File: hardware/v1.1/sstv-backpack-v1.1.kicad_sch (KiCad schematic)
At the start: 23 parts, among them J1 Conn_01x03_Pin, J2 Conn_01x02_Pin, J4 USB_C_Receptacle_USB2.0_14P, Q2 2N3904, SW1 SW_Push, SW2 SLW-1276864-4A-D, U1 ESP32-CAM, U2 FT231XS

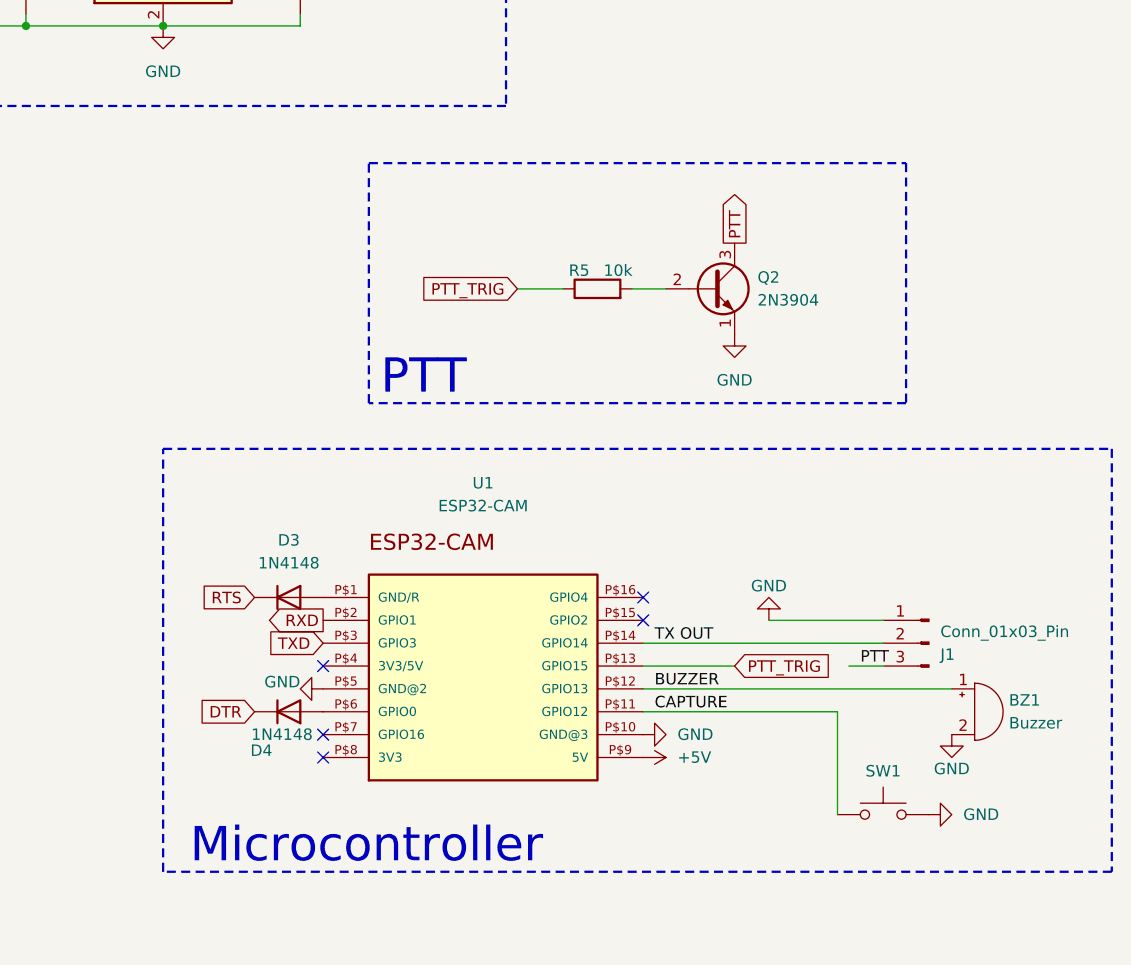
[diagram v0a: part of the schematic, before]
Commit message: Update README and add pull-down resistors for PTT
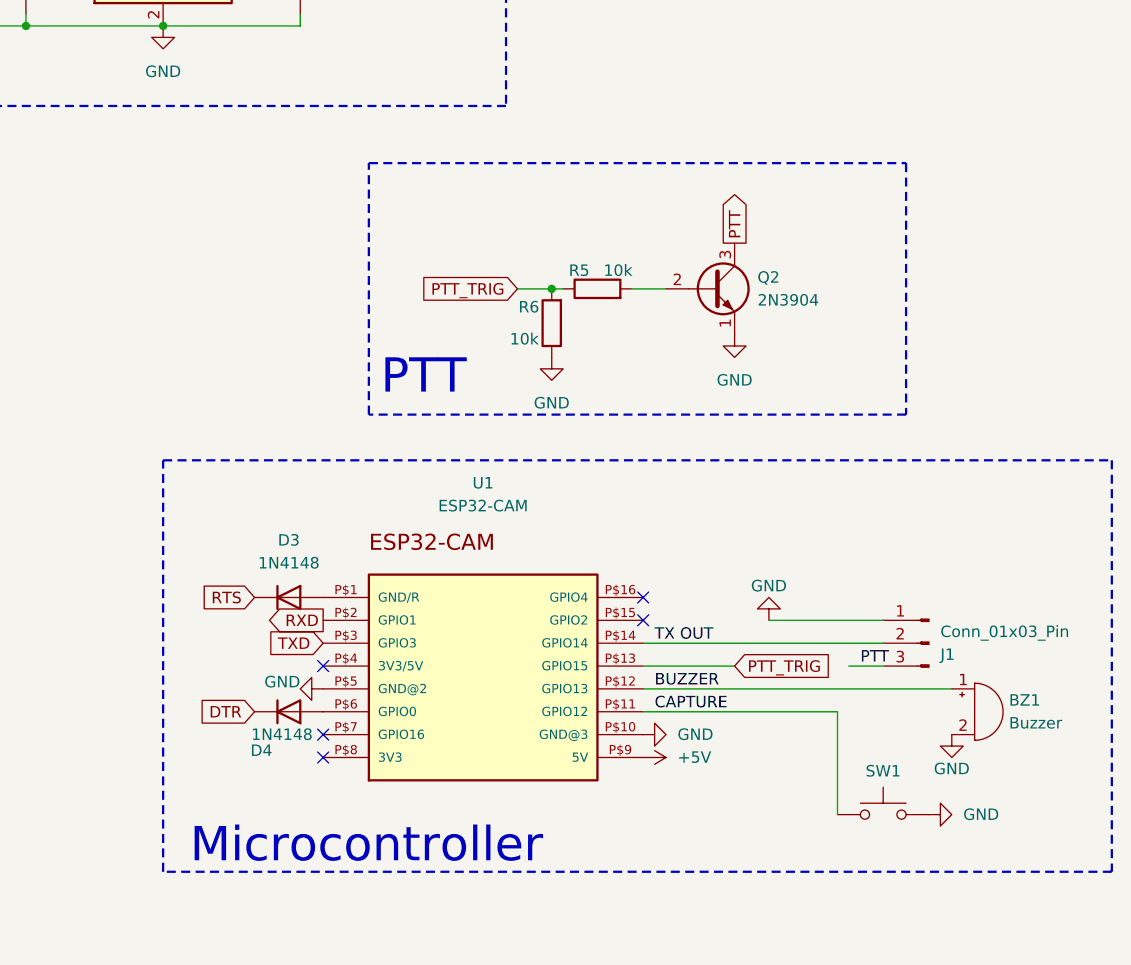
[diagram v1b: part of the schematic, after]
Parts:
- added R6: 10k, Resistor_THT:R_Axial_DIN0207_L6.3mm_D2.5mm_P7.62mm_Horizontal, symbol Device:R
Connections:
- net GND: now also R6.1
- net PTT_TRIG: now also R6.2
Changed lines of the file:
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@@
 	)
 	(rectangle
-		(start 163.83 109.22)
+		(start 163.83 110.49)
 		(end 269.24 156.21)
 		(stroke
@@
 	(rectangle
 		(start 186.69 77.47)
-		(end 246.38 104.14)
+		(end 246.38 105.41)
 		(stroke
 			(width 0.25)
@@
 	)
 	(junction
+		(at 207.01 91.44)
+		(diameter 0)
+		(color 0 0 0 0)
+	)
+	(junction
 		(at 179.07 52.07)
 		(diameter 0)
@@
 	(wire
 		(pts
+			(xy 207.01 91.44) (xy 208.28 91.44)
+		)
+		(stroke
+			(width 0)
+			(type default)
+		)
+	)
+	(wire
+		(pts
 			(xy 69.85 119.38) (xy 72.39 119.38)
 		)
@@
 	(wire
 		(pts
-			(xy 203.2 91.44) (xy 208.28 91.44)
+			(xy 203.2 91.44) (xy 207.01 91.44)
 		)
 		(stroke
@@
 				(path "/29ea68c4-1664-4e2a-8c4b-cdbccd245911"
 					(reference "#PWR017")
+					(unit 1)
+				)
+			)
+		)
+	)
+	(symbol
+		(lib_id "Device:R")
+		(at 207.01 95.25 180)
+		(unit 1)
+		(exclude_from_sim no)
+		(in_bom yes)
+		(on_board yes)
+		(dnp no)
+		(property "Reference" "R6"
+			(at 204.47 93.472 0)
+			(effects
+				(font
+					(size 1.27 1.27)
+				)
+			)
+		)
+		(property "Value" "10k"
+			(at 203.962 97.028 0)
+			(effects
+				(font
+					(size 1.27 1.27)
+				)
+			)
+		)
+		(property "Footprint" "Resistor_THT:R_Axial_DIN0207_L6.3mm_D2.5mm_P7.62mm_Horizontal"
+			(at 208.788 95.25 90)
+			(effects
+				(font
+					(size 1.27 1.27)
+				)
+				(hide yes)
+			)
+		)
+		(property "Datasheet" "~"
+			(at 207.01 95.25 0)
+			(effects
+				(font
+					(size 1.27 1.27)
+				)
+				(hide yes)
+			)
+		)
+		(property "Description" "Resistor"
+			(at 207.01 95.25 0)
+			(effects
+				(font
+					(size 1.27 1.27)
+				)
+				(hide yes)
+			)
+		)
+		(pin "1"
+		)
+		(pin "2"
+		)
+		(instances
+			(project "sstv-backpack-v1.1"
+				(path "/29ea68c4-1664-4e2a-8c4b-cdbccd245911"
+					(reference "R6")
 					(unit 1)
 				)
@@
 					(unit 1)
 				)
+			)
+		)
+	)
+	(symbol
+		(lib_id "power:GND")
+		(at 207.01 99.06 0)
+		(unit 1)
+		(exclude_from_sim no)
+		(in_bom yes)
+		(on_board yes)
+		(dnp no)
+		(fields_autoplaced yes)
+		(property "Reference" "#PWR08"
+			(at 207.01 105.41 0)
+			(effects
+				(font
+					(size 1.27 1.27)
+				)
+				(hide yes)
+			)
+		)
+		(property "Value" "GND"
+			(at 207.01 104.14 0)
+			(effects
+				(font
+					(size 1.27 1.27)
+				)
+			)
+		)
+		(property "Footprint" ""
+			(at 207.01 99.06 0)
+			(effects
+				(font
+					(size 1.27 1.27)
+				)
+				(hide yes)
+			)
+		)
+		(property "Datasheet" ""
+			(at 207.01 99.06 0)
+			(effects
+				(font
+					(size 1.27 1.27)
+				)
+				(hide yes)
+			)
+		)
+		(property "Description" "Power symbol creates a global label with name \"GND\" , ground"
+			(at 207.01 99.06 0)
+			(effects
+				(font
+					(size 1.27 1.27)
+				)
+				(hide yes)
+			)
+		)
+		(pin "1"
+		)
+		(instances
+			(project "sstv-backpack-v1.1"
+				(path "/29ea68c4-1664-4e2a-8c4b-cdbccd245911"
+					(reference "#PWR08")
+					(unit 1)
+				)
